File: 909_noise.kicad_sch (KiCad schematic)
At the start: 20 parts, among them J1 Conn_01x02_Pin, J2 Conn_01x03_Pin, J3 Conn_ARM_JTAG_SWD_10, SW1 PTS645SM43SMTR92 LFS, U1 STM32G030J6Mx, U2 L78L33ABUTR, U3 TLV7211A

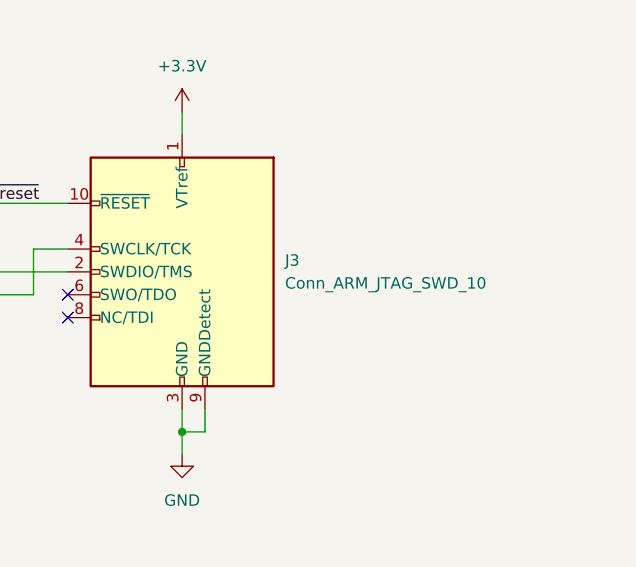
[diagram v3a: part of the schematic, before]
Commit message: change to cheaper debug connector
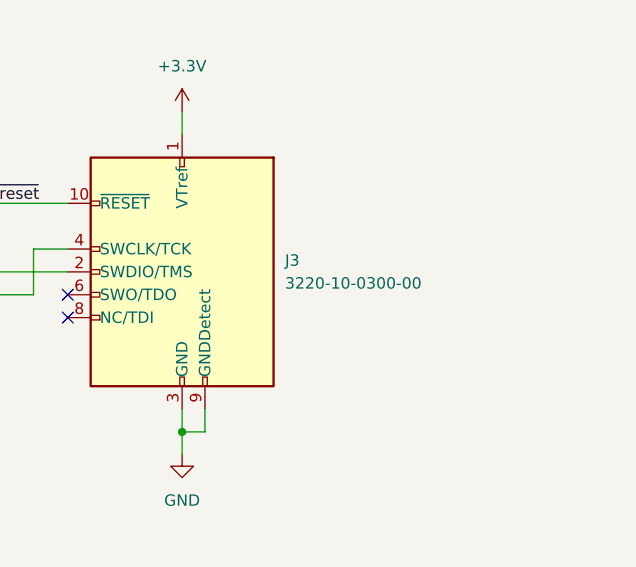
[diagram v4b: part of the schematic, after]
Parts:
- J3: value Conn_ARM_JTAG_SWD_10 -> 3220-10-0300-00; footprint Connector_PinHeader_1.27mm:PinHeader_2x05_P1.27mm_Vertical_SMD -> Connector_CNC_Tech:CNC_Tech_3220-10-0300-00_2x05_P1.27mm_Vertical
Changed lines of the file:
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@@
 			)
 		)
-		(property "Value" "Conn_ARM_JTAG_SWD_10"
+		(property "Value" "3220-10-0300-00"
 			(at 231.14 91.4399 0)
 			(effects
@@
 			)
 		)
-		(property "Footprint" "Connector_PinHeader_1.27mm:PinHeader_2x05_P1.27mm_Vertical_SMD"
+		(property "Footprint" "Connector_CNC_Tech:CNC_Tech_3220-10-0300-00_2x05_P1.27mm_Vertical"
 			(at 219.71 90.17 0)
 			(effects

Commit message: cleanup footprint attributes between pcb and sch
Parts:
- LOGO1, LOGO2: now left out of the parts list
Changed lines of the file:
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@@
 		(unit 1)
 		(exclude_from_sim no)
-		(in_bom yes)
+		(in_bom no)
 		(on_board yes)
 		(dnp no)
@@
 		(unit 1)
 		(exclude_from_sim no)
-		(in_bom yes)
-		(on_board yes)
-		(dnp no)
+		(in_bom no)
+		(on_board yes)
+		(dnp no)

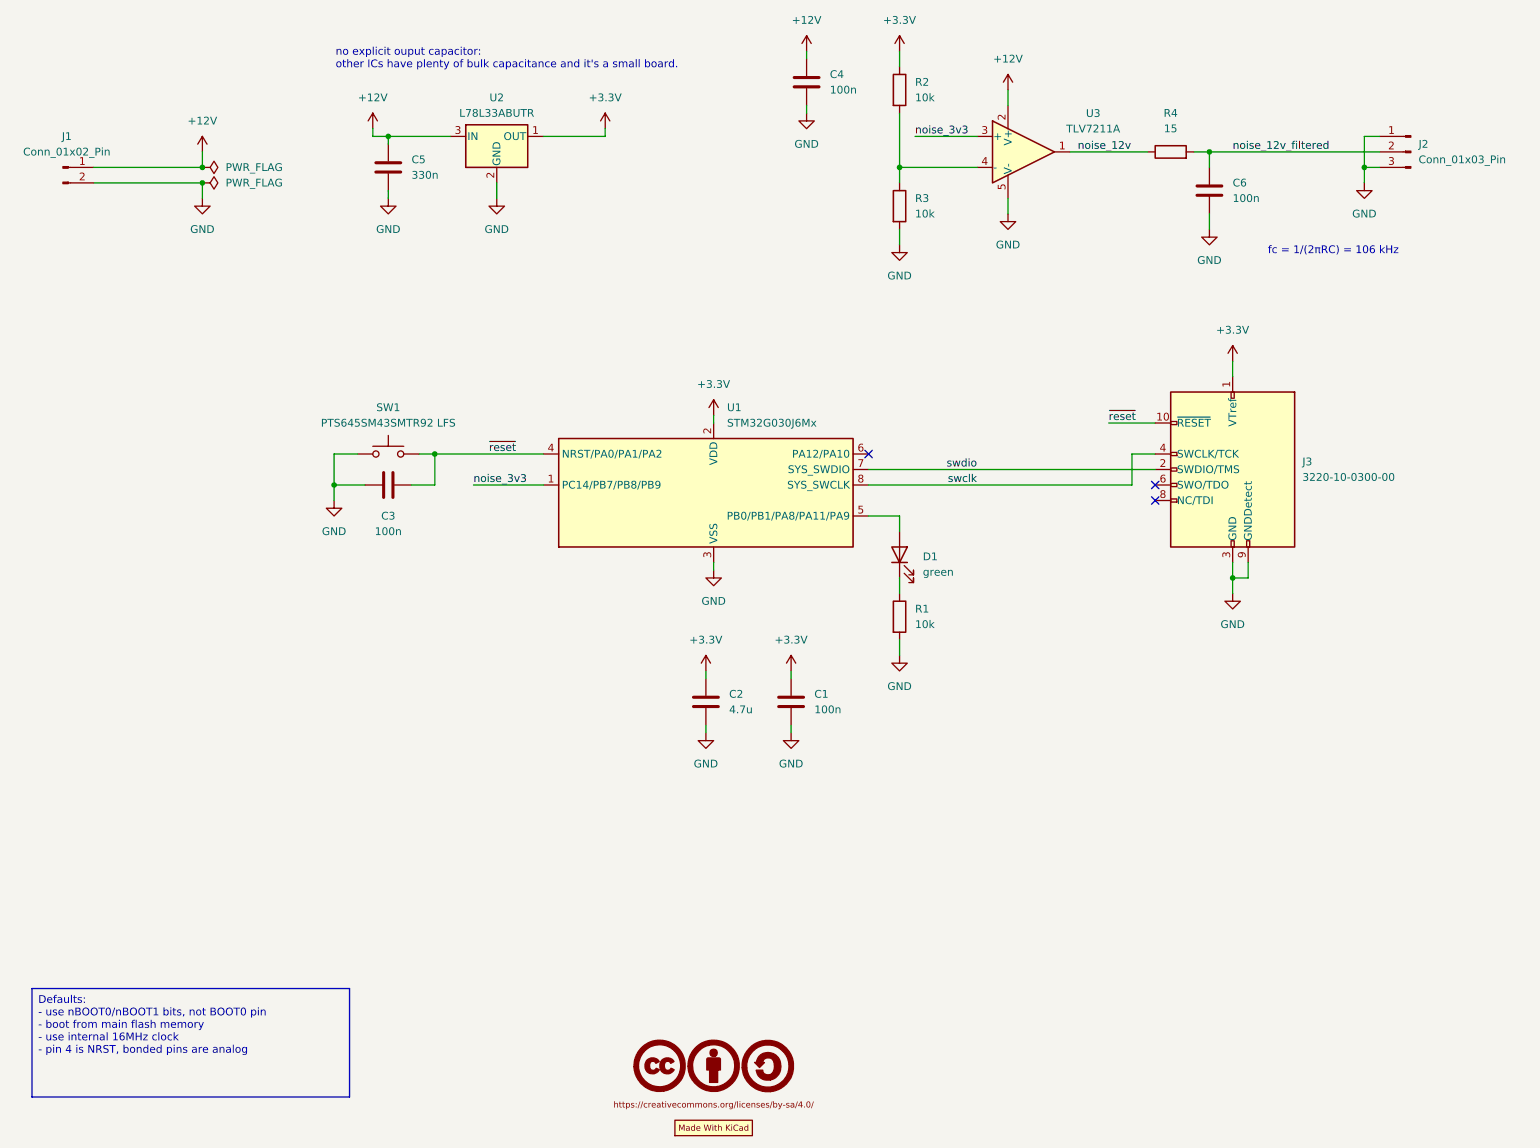
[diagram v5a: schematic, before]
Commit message: swap symbols for specified symbols from dblib
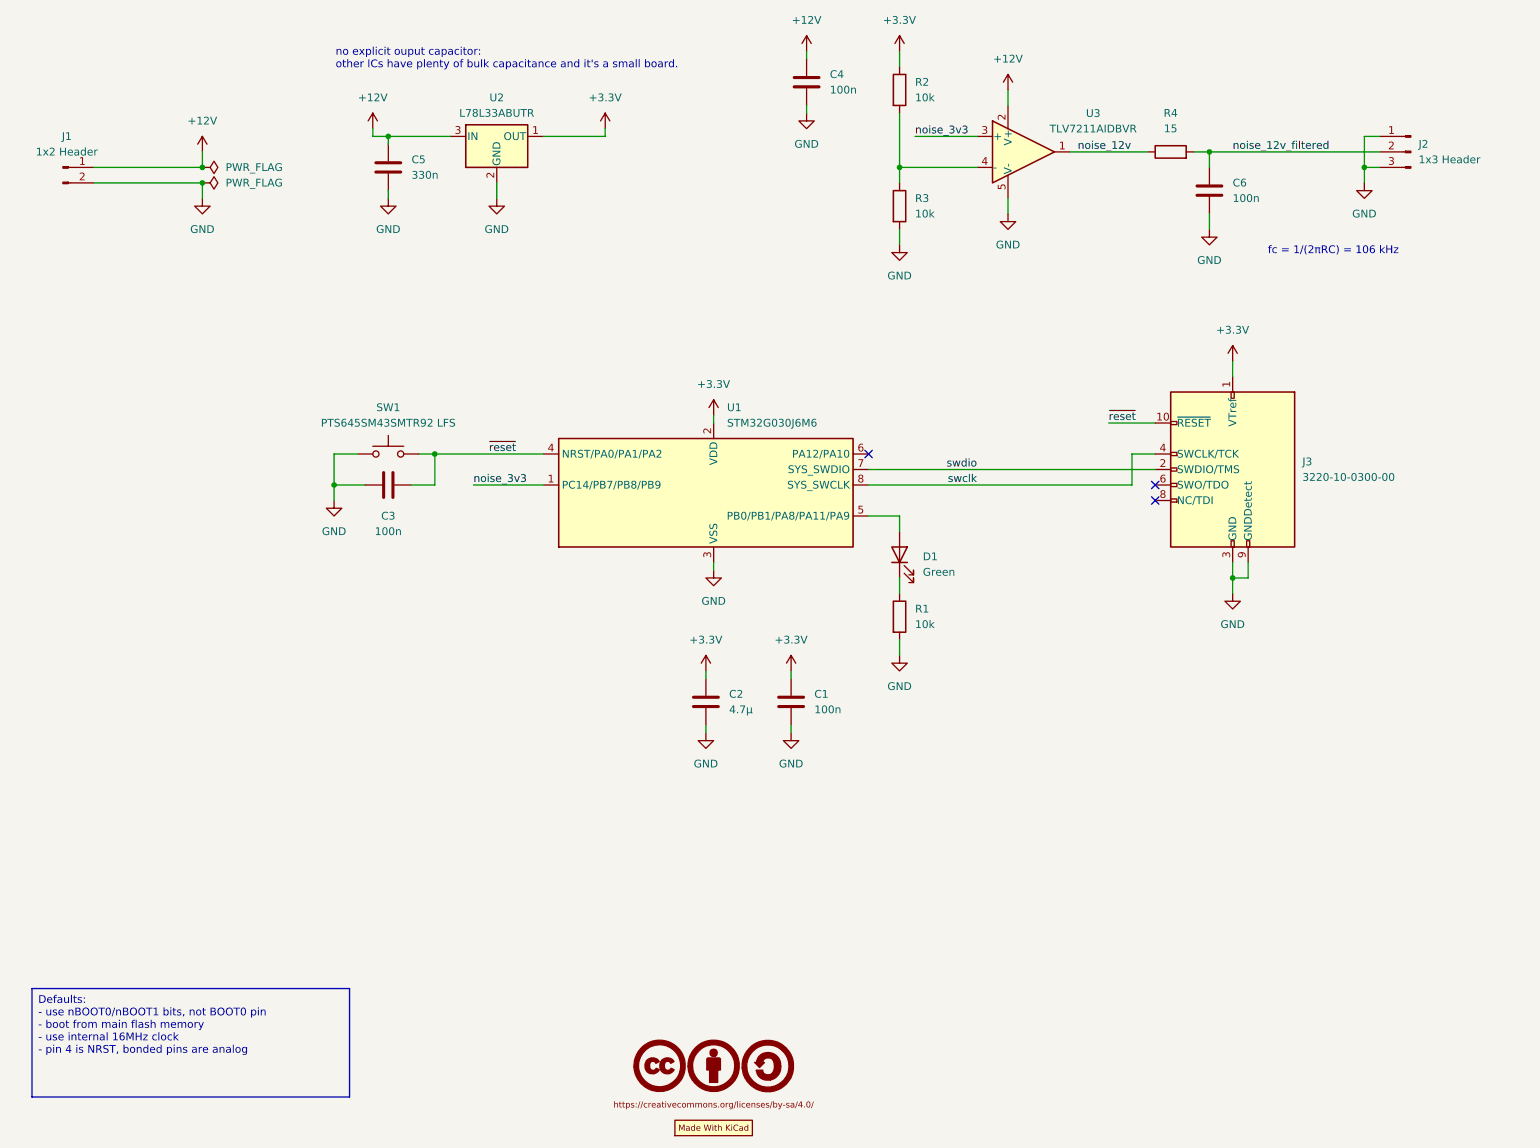
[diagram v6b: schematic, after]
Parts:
- C1, C3, C4, C6: value 100n -> ${Capacitance}; symbol Device:C -> gkeeth-dblib:Capacitors/C0085; Capacitance (none) -> 100n; Dielectric (none) -> X7R; Package (none) -> 0603; Tolerance (none) -> 10%; Voltage Rating (none) -> 50V
- C2: value 4.7u -> ${Capacitance}; symbol Device:C -> gkeeth-dblib:Capacitors/C0213; Capacitance (none) -> 4.7μ; Dielectric (none) -> X7R; Package (none) -> 0805; Tolerance (none) -> 10%; Voltage Rating (none) -> 50V
- C5: value 330n -> ${Capacitance}; symbol Device:C -> gkeeth-dblib:Capacitors/C0091; Capacitance (none) -> 330n; Dielectric (none) -> X7R; Package (none) -> 0603; Tolerance (none) -> 10%; Voltage Rating (none) -> 50V
- D1: value green -> ${Color}; symbol Device:LED -> gkeeth-dblib:LEDs/LED0002; Color (none) -> Green; DPN 1 (none) -> 160-1446-1-ND; Distributor 1 (none) -> Digikey; Forward Voltage (none) -> 2V; MPN (none) -> LTST-C191KGKT; Manufacturer (none) -> Lite-On Inc.; Package (none) -> 0603
- J1: value Conn_01x02_Pin -> 1x2 Header; symbol Connector:Conn_01x02_Pin -> gkeeth-dblib:Connectors/CONN0002; Package (none) -> Header
- J2: value Conn_01x03_Pin -> 1x3 Header; symbol Connector:Conn_01x03_Pin -> gkeeth-dblib:Connectors/CONN0003; Package (none) -> Header
- J3: value 3220-10-0300-00 -> ${MPN}; symbol Connector:Conn_ARM_JTAG_SWD_10 -> gkeeth-dblib:Connectors/CONN0017; DPN 1 (none) -> 1175-1629-ND; Distributor 1 (none) -> Digikey; MPN (none) -> 3220-10-0300-00; Manufacturer (none) -> CNC Tech; Package (none) -> Header
- LOGO1: value CC-BY-SA_0.33in -> CC-BY-SA; symbol Creative_Commons:CC-BY-SA_0.33in -> gkeeth-dblib:Graphics/GRAPHIC0002; Package (none) -> graphic
- LOGO2: value Logo_MadeWithKiCad -> Made With KiCad; symbol Graphic_gkeeth:Logo_MadeWithKiCad -> gkeeth-dblib:Graphics/GRAPHIC0001; Package (none) -> graphic
- R1, R2, R3: value 10k -> ${Resistance}; symbol Device:R -> gkeeth-dblib:Resistors/R0386; Composition (none) -> Thin Film; Package (none) -> 0603; Power Rating (none) -> 0.1W; Resistance (none) -> 10k; Tolerance (none) -> 1%
- R4: value 15 -> ${Resistance}; symbol Device:R -> gkeeth-dblib:Resistors/R0115; Composition (none) -> Thin Film; Package (none) -> 0603; Power Rating (none) -> 0.1W; Resistance (none) -> 15; Tolerance (none) -> 1%
- SW1: value PTS645SM43SMTR92 LFS -> ${MPN}; symbol Switch:SW_Push -> gkeeth-dblib:Switches/SW0001; DPN 1 (none) -> CKN9112CT-ND; Distributor 1 (none) -> Digikey; MPN (none) -> PTS645SM43SMTR92 LFS; Manufacturer (none) -> C&K; Package (none) -> PTS645
- U1: value STM32G030J6Mx -> ${MPN}; symbol MCU_ST_STM32G0:STM32G030J6Mx -> gkeeth-dblib:Microcontrollers/MCU0002; Core (none) -> ARM Cortex-M0; DPN 1 (none) -> 497-STM32G030J6M6-ND; Distributor 1 (none) -> Digikey; MPN (none) -> STM32G030J6M6; Manufacturer (none) -> STMicroelectronics; Package (none) -> 8-SOIC; Speed (none) -> 64MHz
- U2: value L78L33ABUTR -> ${MPN}; symbol Regulator_Linear:L78L33_SOT89 -> gkeeth-dblib:Voltage Regulators/VREG0002; DPN 1 (none) -> 497-7286-1-ND; Distributor 1 (none) -> Digikey; MPN (none) -> L78L33ABUTR; Manufacturer (none) -> STMicroelectronics; Output Current (none) -> 100mA; Output Voltage (none) -> 3.3V; Package (none) -> SOT-89-3
- U3: value TLV7211A -> ${MPN}; symbol Comparator:MCP6561R -> gkeeth-dblib:Comparators/COMP0001; DPN 1 (none) -> 296-21866-1-ND; Distributor 1 (none) -> Digikey; MPN (none) -> TLV7211AIDBVR; Manufacturer (none) -> Texas Instruments; Number of Units (none) -> 1; Output Type (none) -> Push-Pull; Package (none) -> SC-74A, SOT-753

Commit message: routed with single-supply +12V on opamp
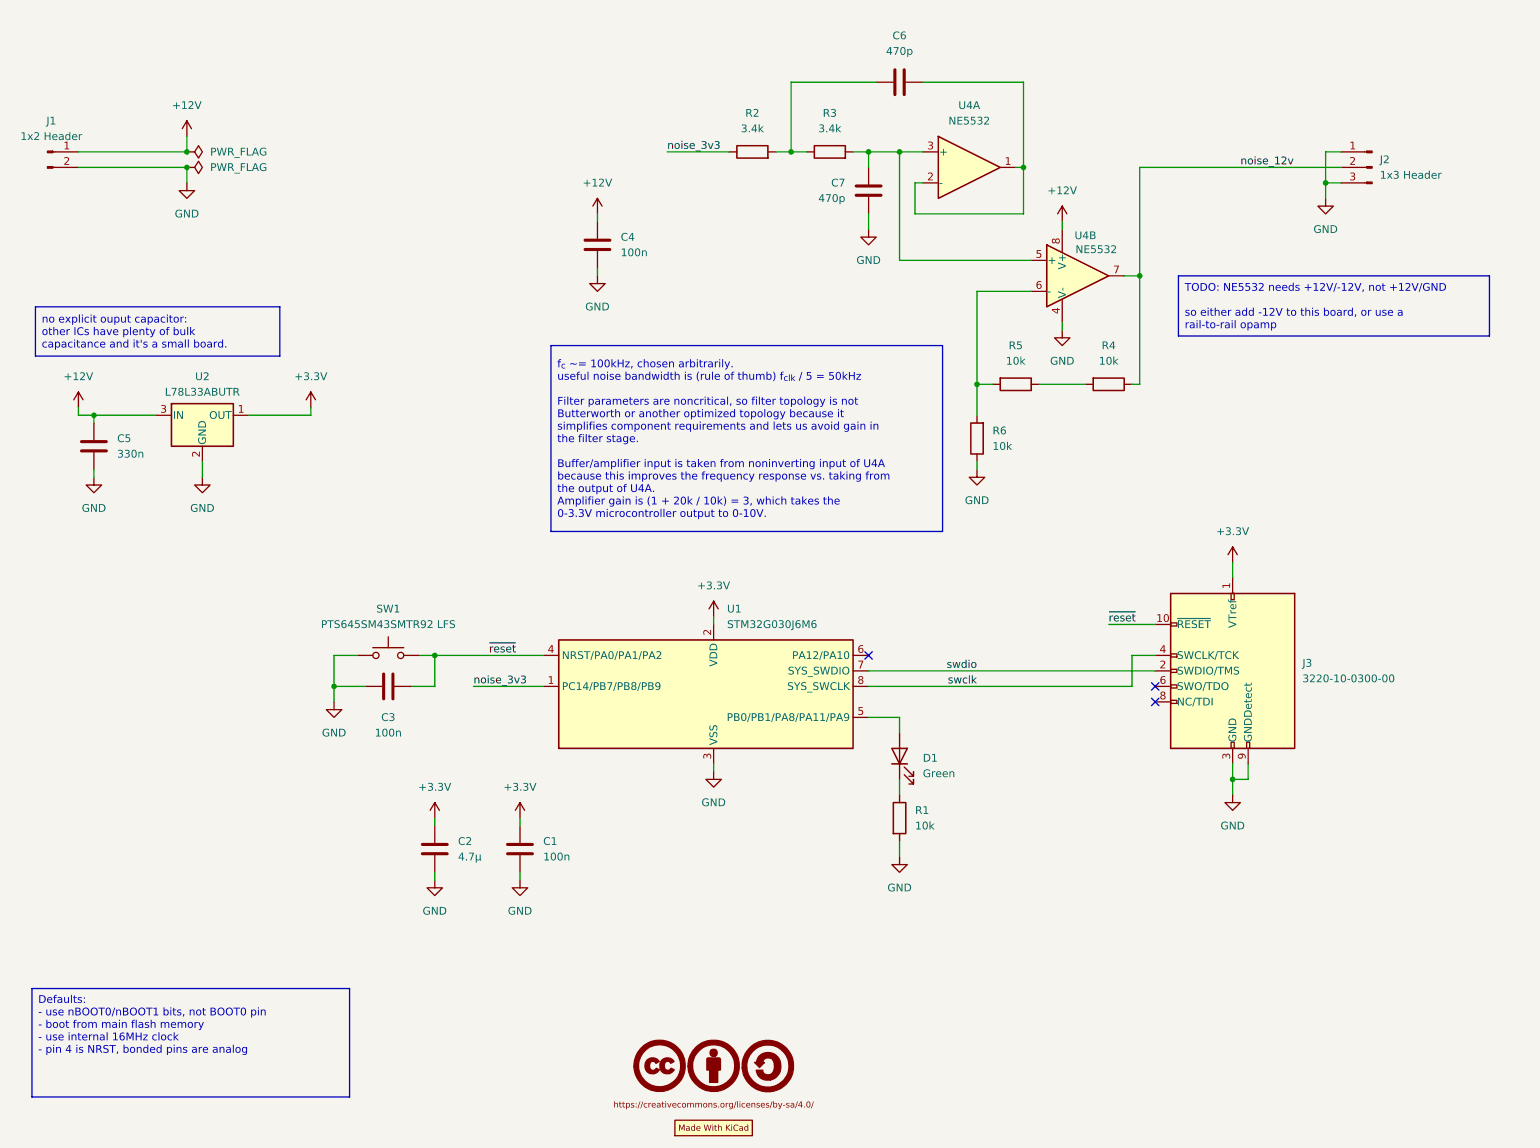
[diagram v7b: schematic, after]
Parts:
- removed C6: ${Capacitance}, Capacitor_SMD:C_0603_1608Metric, symbol gkeeth-dblib:Capacitors/C0085
- removed U3: ${MPN}, Package_TO_SOT_SMD:SOT-23-5, symbol gkeeth-dblib:Comparators/COMP0001
- added C6, C7: ${Capacitance}, Capacitor_SMD:C_0603_1608Metric, symbol gkeeth-dblib:Capacitors/C0041
- added R5, R6: ${Resistance}, Resistor_SMD:R_0603_1608Metric, symbol gkeeth-dblib:Resistors/R0386
- added U4: NE5532, Package_SO:SOIC-8_3.9x4.9mm_P1.27mm, symbol Amplifier_Operational:NE5532
- R2, R3: symbol gkeeth-dblib:Resistors/R0386 -> gkeeth-dblib:Resistors/R0341; Resistance 10k -> 3.4k
- R4: symbol gkeeth-dblib:Resistors/R0115 -> gkeeth-dblib:Resistors/R0386; Resistance 15 -> 10k
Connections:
- net +12V: now also U4.8 (V+)
- net +3.3V: no longer R2.1
- net GND: now also C7.2, R6.1, U4.4 (V-); no longer R3.2
- net noise_12v: now also J2.2 (Pin_2), U4.7
- net noise_3v3: now also R2.1
- net at R2.2, R3.1: now also C6.1
- net noise_12v_filtered: no longer names the net of R4.2
- net noise_12v_filtered: now also R5.1; no longer J2.2 (Pin_2)
- new net: C7.1, R3.2, U4.3 (+), U4.5 (+)
- new net: R5.2, R6.2, U4.6 (-)
- new net: C6.2, U4.1, U4.2 (-)
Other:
- note removed: "fc = 1/(2πRC) = 106 kHz"
- note removed: "no explicit ouput capacitor: other ICs have plenty of bulk capacitance and it's a small board."
- moved on the sheet: C1, C2, C3, C4, C5, D1, J1, J2, J3, R1, R2, R3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

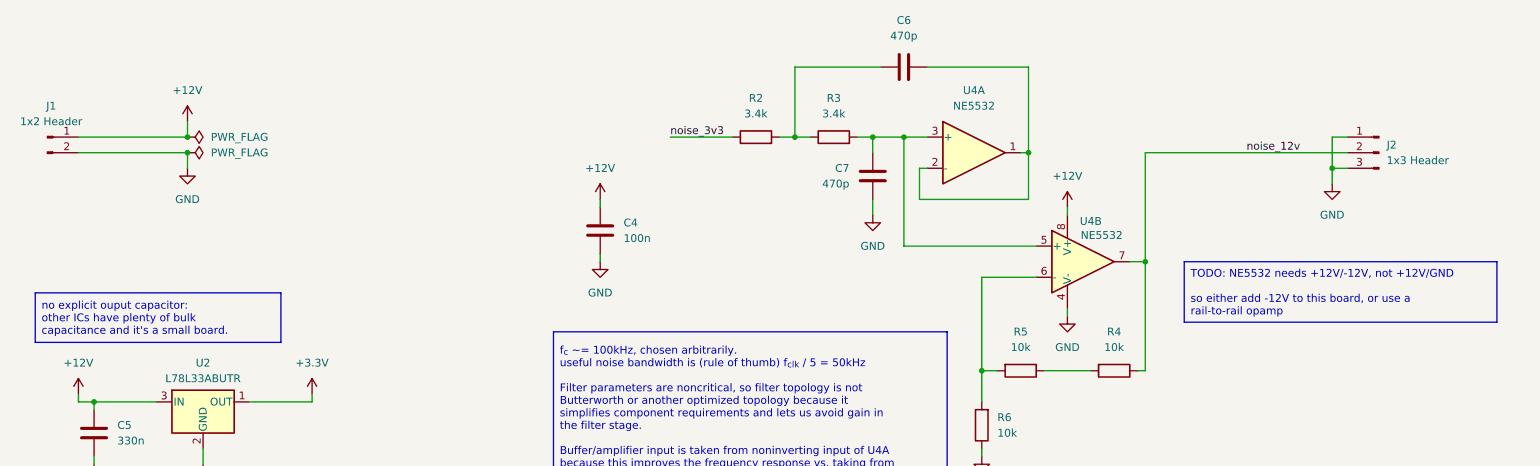
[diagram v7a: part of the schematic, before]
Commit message: add -12V to opamp
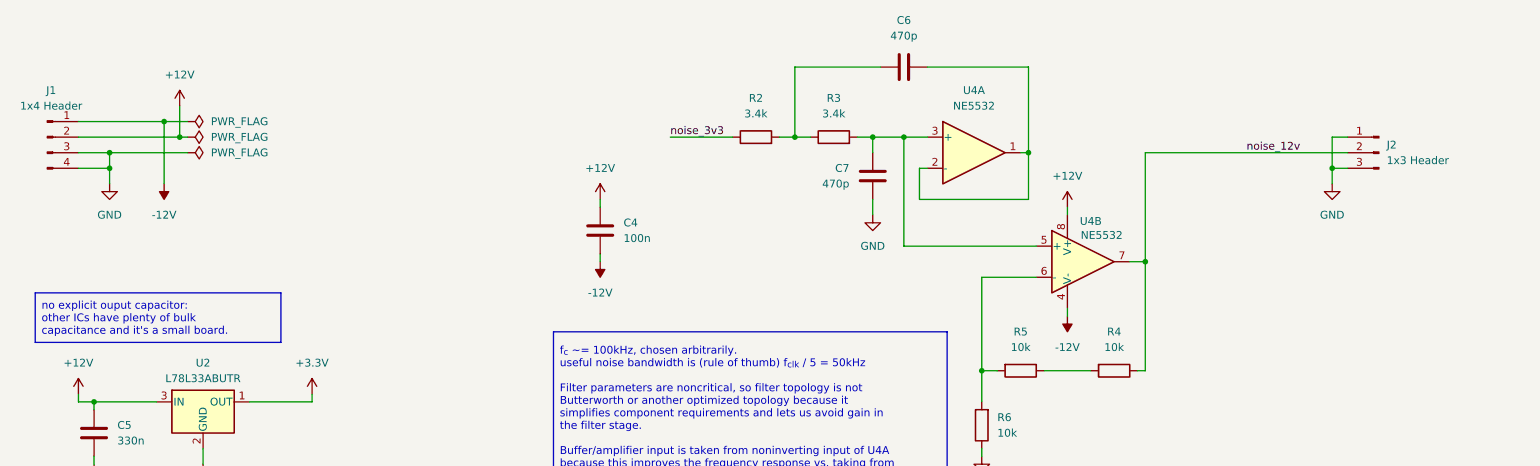
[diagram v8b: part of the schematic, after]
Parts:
- removed J1: 1x2 Header, Connector_PinHeader_2.54mm:PinHeader_1x02_P2.54mm_Vertical, symbol gkeeth-dblib:Connectors/CONN0002
- added J1: 1x4 Header, Connector_PinHeader_2.54mm:PinHeader_1x04_P2.54mm_Vertical, symbol gkeeth-dblib:Connectors/CONN0004
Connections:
- net +12V: now also J1.2 (Pin_2)
- net GND: now also J1.3 (Pin_3), J1.4 (Pin_4); no longer C4.1, U4.4 (V-)
- new net -12V: C4.1, J1.1 (Pin_1), U4.4 (V-)
